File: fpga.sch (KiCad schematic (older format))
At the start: 58 parts, among them P1 JTAG, SW2 BTN0, U10 S25FL216K, U12 TLV70012, U13 TLV70025, U14 TLV70012, U2 EP4CE15E22

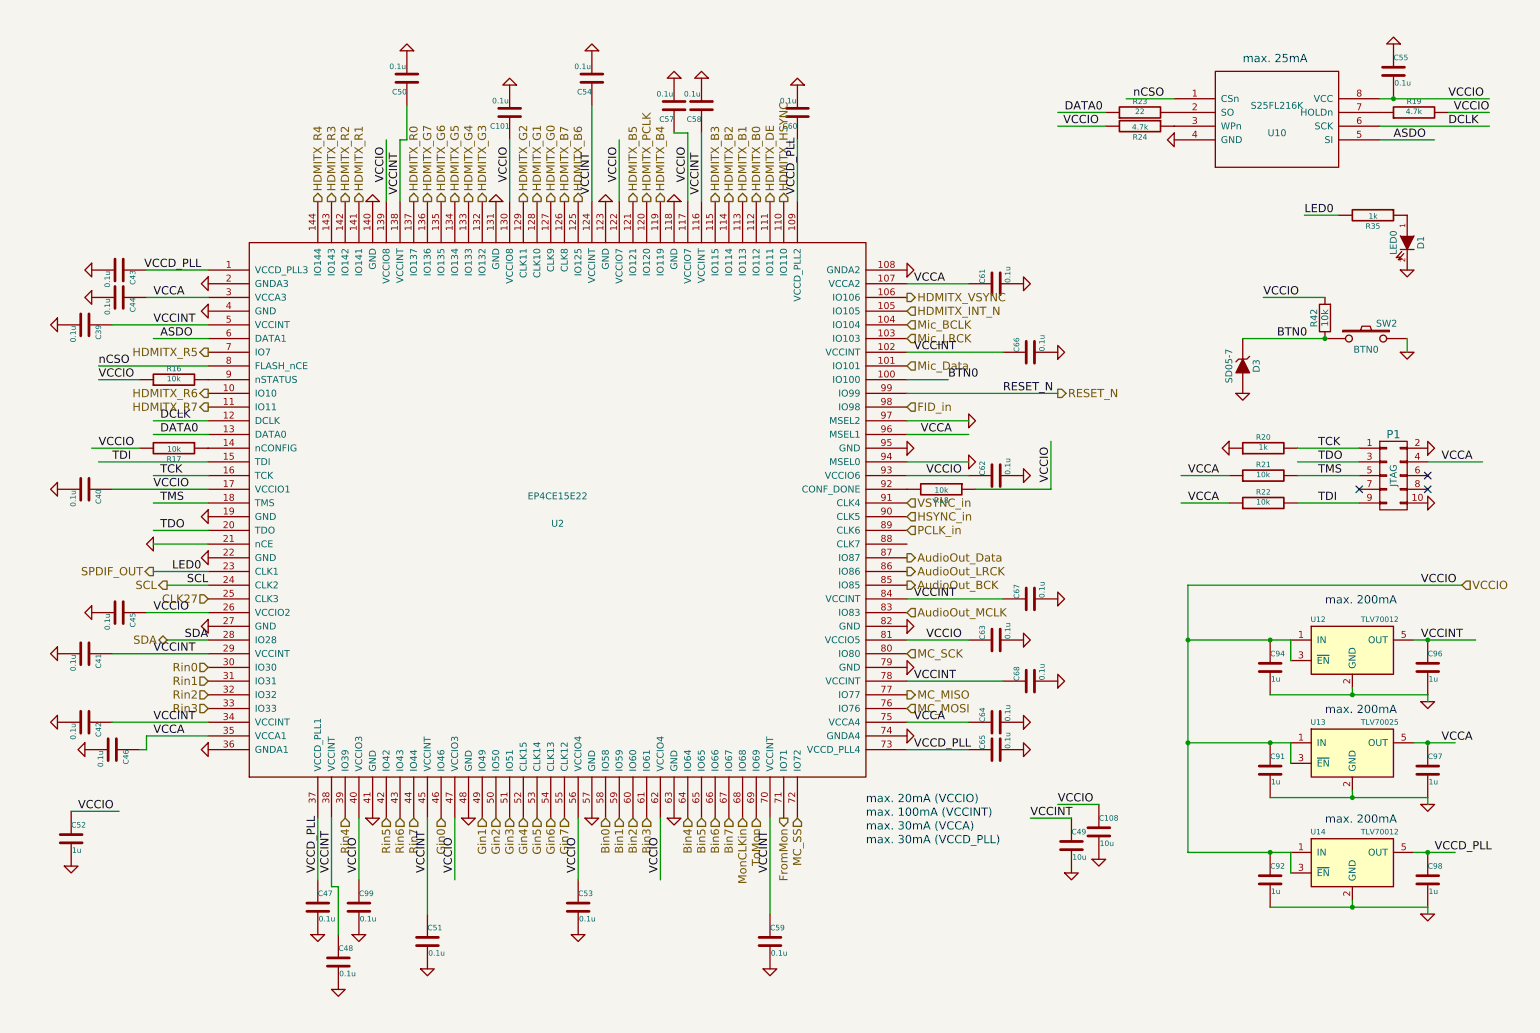
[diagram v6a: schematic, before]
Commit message: add adc
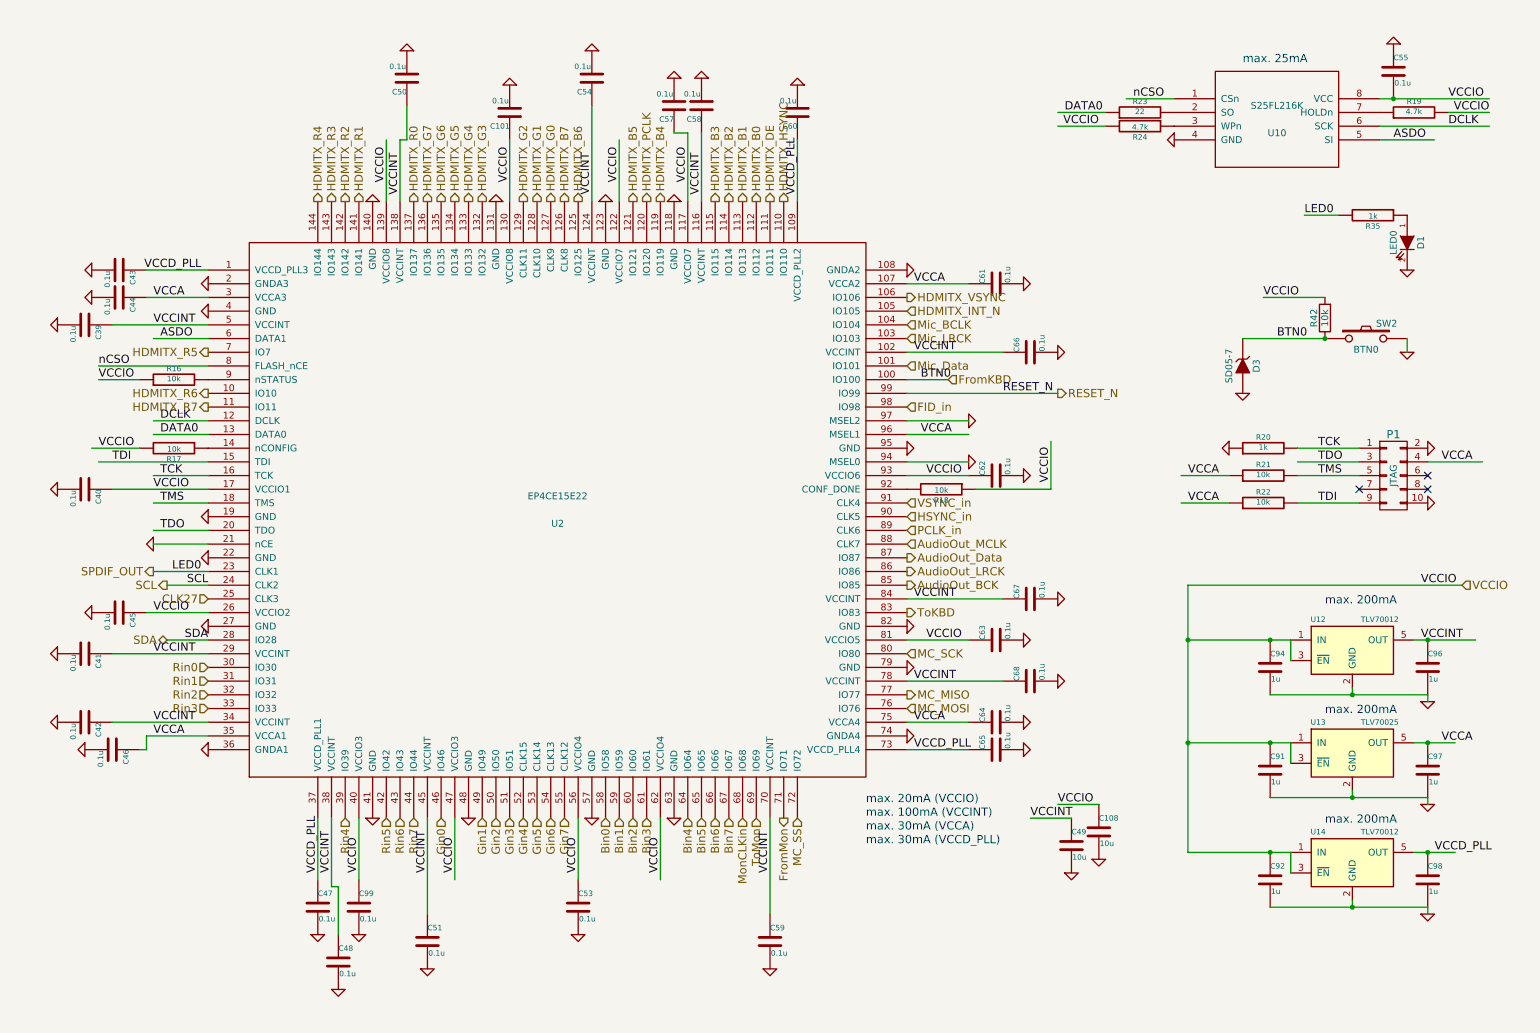
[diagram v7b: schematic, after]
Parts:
- removed C52: 1u, Capacitor_SMD:C_0603_1608Metric_Pad1.05x0.95mm_HandSolder, symbol ossc_board-rescue:C-RESCUE-ossc_board
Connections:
- net labels added: FromKBD, ToKBD
- wire segments 113 -> 112
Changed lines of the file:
@@
 SCL
-$Comp
-L ossc_board-rescue:C-RESCUE-ossc_board C52
-U 1 1 551863DE
-P 700 6500
-F 0 "C52" H 700 6600 40  0000 L CNN
-F 1 "1u" H 706 6415 40  0000 L CNN
-F 2 "Capacitor_SMD:C_0603_1608Metric_Pad1.05x0.95mm_HandSolder" H 738 6350 30  0001 C CNN
-F 3 "~" H 700 6500 60  0000 C CNN
-	1    700  6500
-	1    0    0    -1
-$EndComp
-$Comp
-L ossc_board-rescue:GND-RESCUE-ossc_board #PWR068
-U 1 1 551863E4
-P 700 6700
-F 0 "#PWR068" H 700 6700 30  0001 C CNN
-F 1 "GND" H 700 6630 30  0001 C CNN
-F 2 "" H 700 6700 60  0001 C CNN
-F 3 "" H 700 6700 60  0000 C CNN
-	1    700  6700
-	1    0    0    -1
-$EndComp
-Text Label 750  6300 0    60   ~ 0
-VCCIO
 $Comp
 L ossc_board-rescue:C-RESCUE-ossc_board C55
@@
 Wire Wire Line
 	6800 3250 7900 3250
-Wire Wire Line
-	1050 6300 700  6300
 Connection ~ 10350 1100
 Wire Wire Line
@@
 Text Label 9400 2550 0    60   ~ 0
 VCCIO
-Text Label 7100 3150 0    60   ~ 0
+Text Label 6900 3150 0    60   ~ 0
 BTN0
 Wire Wire Line
@@
 Text HLabel 6800 5150 2    60   Input ~ 0
 MC_SCK
-Text HLabel 6800 4850 2    60   Input ~ 0
+Text HLabel 6800 4350 2    60   Input ~ 0
 AudioOut_MCLK
 Text HLabel 6800 4650 2    60   Output ~ 0
@@
 Wire Wire Line
 	7100 3150 6800 3150
+Text HLabel 7100 3150 2    60   Input ~ 0
+FromKBD
+Text HLabel 6800 4850 2    60   Output ~ 0
+ToKBD
 $EndSCHEMATC

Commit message: update PCB
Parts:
- D3: value SD05-7 -> RB160M-30TR; footprint Diode_SMD:D_SOD-323_HandSoldering -> custom_components:D_SOD-123_HandSoldering
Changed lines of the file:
@@
 Text HLabel 6800 3350 2    60   Input ~ 0
 FID_in
-Text HLabel 7900 3250 2    60   Output ~ 0
+Text HLabel 7900 2750 2    60   Output ~ 0
 RESET_N
 Text HLabel 6800 2650 2    60   Input ~ 0
@@
 	10050 5450 10050 5400
 Wire Wire Line
-	8850 5050 9450 5050
-Wire Wire Line
 	9600 5050 9600 5200
 Connection ~ 9450 5050
@@
 	8850 4650 10850 4650
 Wire Wire Line
-	6800 3250 7900 3250
+	6800 2750 7900 2750
 Connection ~ 10350 1100
 Wire Wire Line
@@
 Text Label 9400 2550 0    60   ~ 0
 VCCIO
-Text Label 6900 3150 0    60   ~ 0
+Text Label 7000 5550 0    60   ~ 0
 BTN0
 Wire Wire Line
@@
 Text Notes 6500 6550 0    60   ~ 0
 max. 30mA (VCCD_PLL)
-Text Label 7500 3250 0    60   ~ 0
+Text Label 7500 2750 0    60   ~ 0
 RESET_N
 $Comp
@@
 VCCIO
 $Comp
-L ossc_board-rescue:ZENER D3
-U 1 1 58C560B1
-P 9250 3050
-F 0 "D3" H 9250 3150 50  0000 C CNN
-F 1 "SD05-7" H 9250 2950 50  0000 C CNN
-F 2 "Diode_SMD:D_SOD-323_HandSoldering" H 9250 3050 60  0001 C CNN
-F 3 "" H 9250 3050 60  0000 C CNN
-	1    9250 3050
-	0    1    1    0
-$EndComp
-$Comp
 L ossc_board-rescue:GND-RESCUE-ossc_board #PWR078
 U 1 1 58C561E6
@@
 Text HLabel 5900 6350 3    60   Output ~ 0
 FromMon
-Text HLabel 6000 6350 3    60   Input ~ 0
+Text HLabel 6800 4650 2    60   Input ~ 0
 MC_SS
-Text HLabel 6800 5550 2    60   Input ~ 0
+Text HLabel 6800 4850 2    60   Input ~ 0
 MC_MOSI
 Text HLabel 6800 5450 2    60   Output ~ 0
@@
 Text HLabel 6800 5150 2    60   Input ~ 0
 MC_SCK
+Text HLabel 6800 2850 2    60   Input ~ 0
+AudioOut_MCLK
+Text HLabel 6800 3250 2    60   Output ~ 0
+AudioOut_BCK
+Text HLabel 6800 3150 2    60   Output ~ 0
+AudioOut_LRCK
+Text HLabel 6800 3050 2    60   Output ~ 0
+AudioOut_Data
+Text HLabel 6800 4550 2    60   Input ~ 0
+Mic_BCLK
 Text HLabel 6800 4350 2    60   Input ~ 0
-AudioOut_MCLK
-Text HLabel 6800 4650 2    60   Output ~ 0
-AudioOut_BCK
-Text HLabel 6800 4550 2    60   Output ~ 0
-AudioOut_LRCK
-Text HLabel 6800 4450 2    60   Output ~ 0
-AudioOut_Data
-Text HLabel 6800 2750 2    60   Input ~ 0
-Mic_BCLK
-Text HLabel 6800 2850 2    60   Input ~ 0
 Mic_LRCK
-Text HLabel 6800 3050 2    60   Input ~ 0
+Text HLabel 6800 4450 2    60   Input ~ 0
 Mic_Data
 Text HLabel 1300 4550 0    60   Output ~ 0
 SPDIF_OUT
-Wire Wire Line
-	7100 3150 6800 3150
-Text HLabel 7100 3150 2    60   Input ~ 0
+Text HLabel 7300 5550 2    60   Input ~ 0
 FromKBD
-Text HLabel 6800 4850 2    60   Output ~ 0
+Text HLabel 6000 6350 3    60   Output ~ 0
 ToKBD
+Wire Wire Line
+	6800 5550 7300 5550
+$Comp
+L ossc_board-rescue:ZENER D3
+U 1 1 58C560B1
+P 9250 3050
+F 0 "D3" H 9250 3150 50  0000 C CNN
+F 1 "RB160M-30TR" H 9250 2950 50  0000 C CNN
+F 2 "custom_components:D_SOD-123_HandSoldering" H 9250 3050 60  0001 C CNN
+F 3 "" H 9250 3050 60  0000 C CNN
+	1    9250 3050
+	0    1    1    0
+$EndComp
+Wire Wire Line
+	8850 5050 9450 5050
 $EndSCHEMATC
